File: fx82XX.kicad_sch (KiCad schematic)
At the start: 53 parts, among them J1 VBAT, J2 GND, J4 U1V10F5, J6 Raspberry_Pi_2_3, P1 Power Button, Q1 MMFTP3401, SW1 SW_Push, SW10 SW_Push, SW11 SW_Push, SW12 SW_Push, SW13 SW_Push, SW14 SW_Push, SW15 SW_Push, SW16 SW_Push, SW17 SW_Push, SW18 SW_Push, SW19 SW_Push, SW2 SW_Push, SW20 SW_Push, SW21 SW_Push, SW22 SW_Push, SW23 SW_Push, SW24 SW_Push, SW25 SW_Push, SW26 SW_Push, SW27 SW_Push, SW28 SW_Push, SW29 SW_Push, SW3 SW_Push, SW30 Previous, SW31 SW_Push, SW32 SW_Push, SW33 SW_Push, SW34 SW_Push, SW35 SW_Push, SW36 UpArrow, SW37 SW_Push, SW38 SW_Push, SW39 SW_Push, SW4 SW_Push, SW40 SW_Push, SW41 SW_Push, SW42 Home, SW43 SW_Push, SW44 SW_Push, SW45 SW_Push, SW46 SW_Push, SW47 SW_Push, SW5 SW_Push, SW6 SW_Push, SW7 SW_Push, SW8 SW_Push, SW9 SW_Push

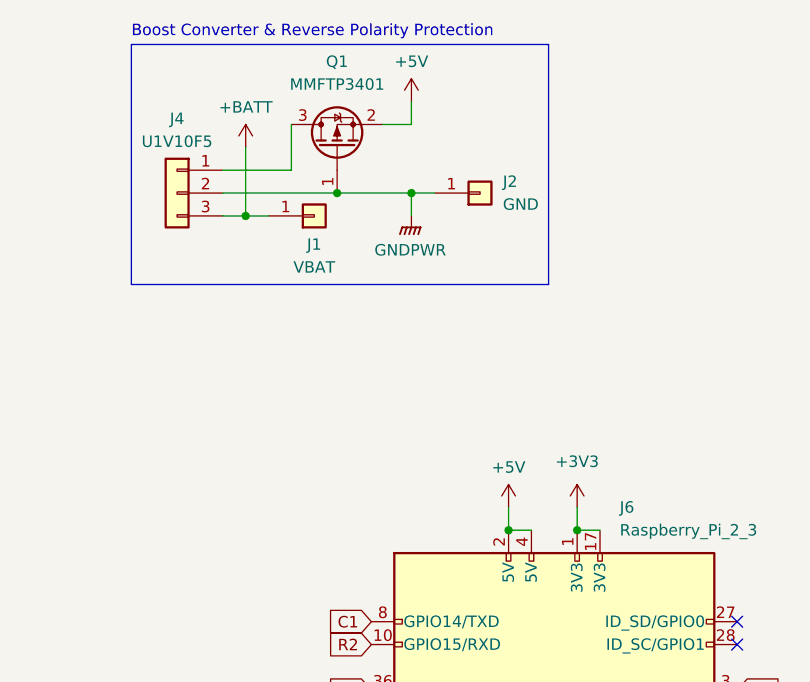
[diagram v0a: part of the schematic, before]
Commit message: Change symbol references
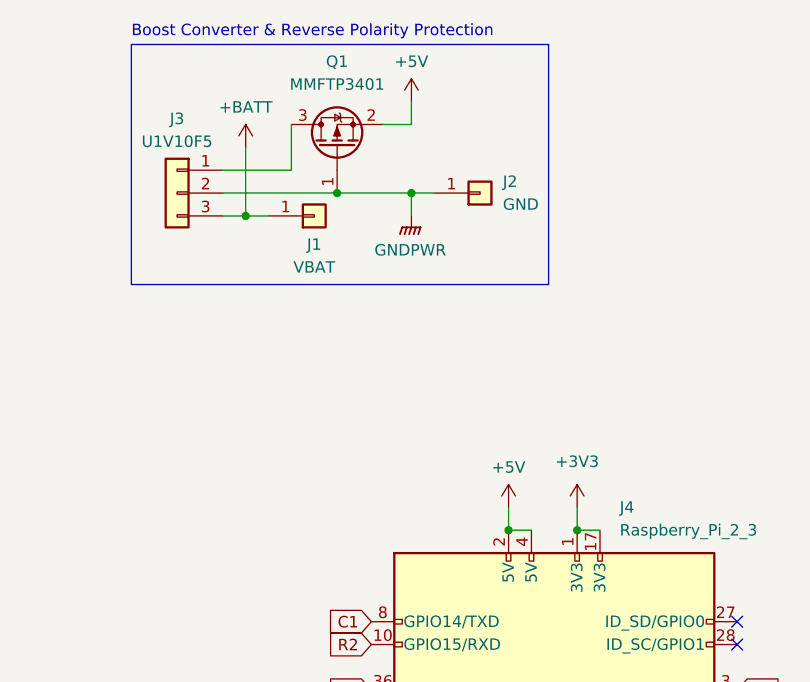
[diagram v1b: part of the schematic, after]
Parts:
- renumbered J4 to J3, J6 to J4
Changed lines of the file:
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@@
   (symbol (lib_id "Connector_Generic:Conn_01x03") (at 132.715 37.465 0) (mirror y) (unit 1)
     (in_bom yes) (on_board yes) (dnp no)
-    (property "Reference" "J4" (at 132.715 29.21 0)
+    (property "Reference" "J3" (at 132.715 29.21 0)
       (effects (font (size 1.27 1.27)))
     )
@@
       (project "fx82XX"
         (path "/d5effe3a-4045-4007-a8c8-6940eeb133a7"
-          (reference "J4") (unit 1)
+          (reference "J3") (unit 1)
         )
       )
@@
   (symbol (lib_id "Connector:Raspberry_Pi_2_3") (at 174.625 107.95 0) (unit 1)
     (in_bom yes) (on_board yes) (dnp no) (fields_autoplaced)
-    (property "Reference" "J6" (at 181.8991 72.39 0)
+    (property "Reference" "J4" (at 181.8991 72.39 0)
       (effects (font (size 1.27 1.27)) (justify left))
     )
@@
       (project "fx82XX"
         (path "/d5effe3a-4045-4007-a8c8-6940eeb133a7"
-          (reference "J6") (unit 1)
-        )
-      )
+          (reference "J4") (unit 1)
+        )
+      )

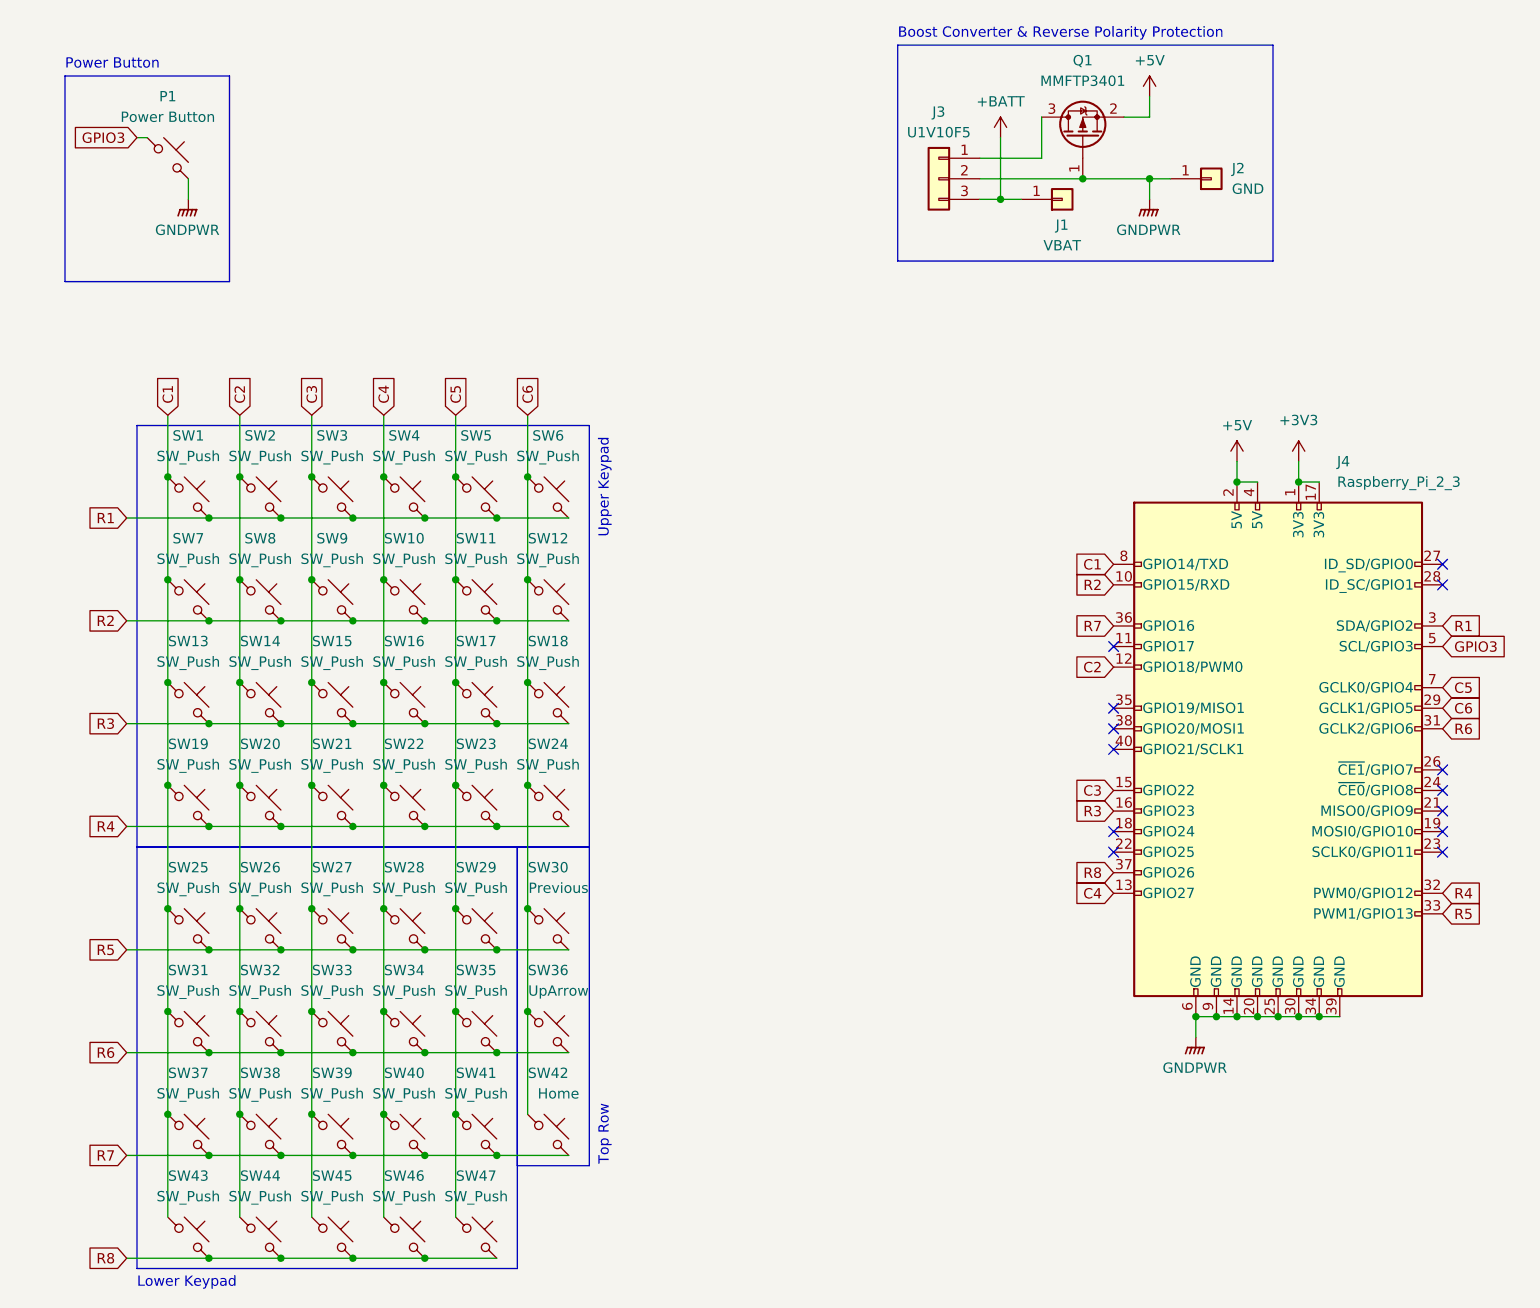
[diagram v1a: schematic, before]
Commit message: Re-route using 2 layers
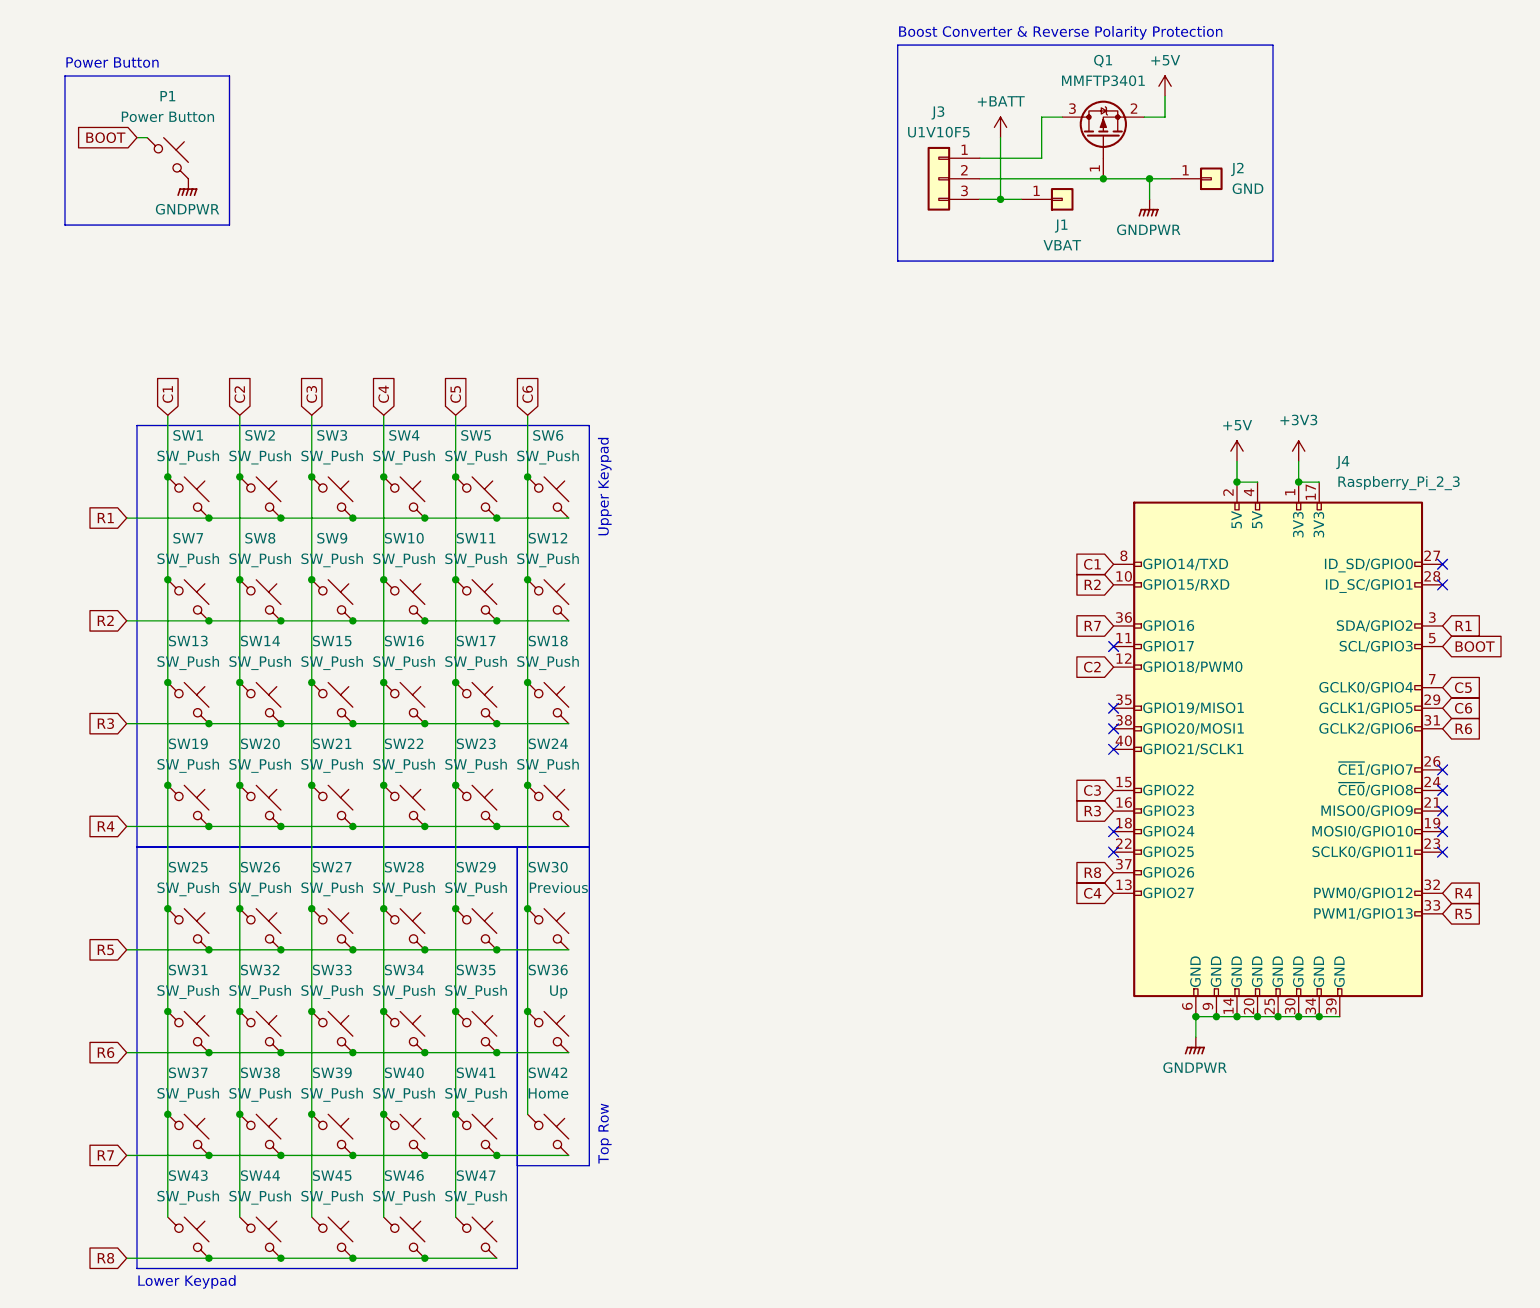
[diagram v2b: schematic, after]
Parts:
- SW36: value UpArrow -> Up
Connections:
- net GPIO3 renamed BOOT
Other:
- moved on the sheet: Q1

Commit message: Redesign PCB to be more accurate and better
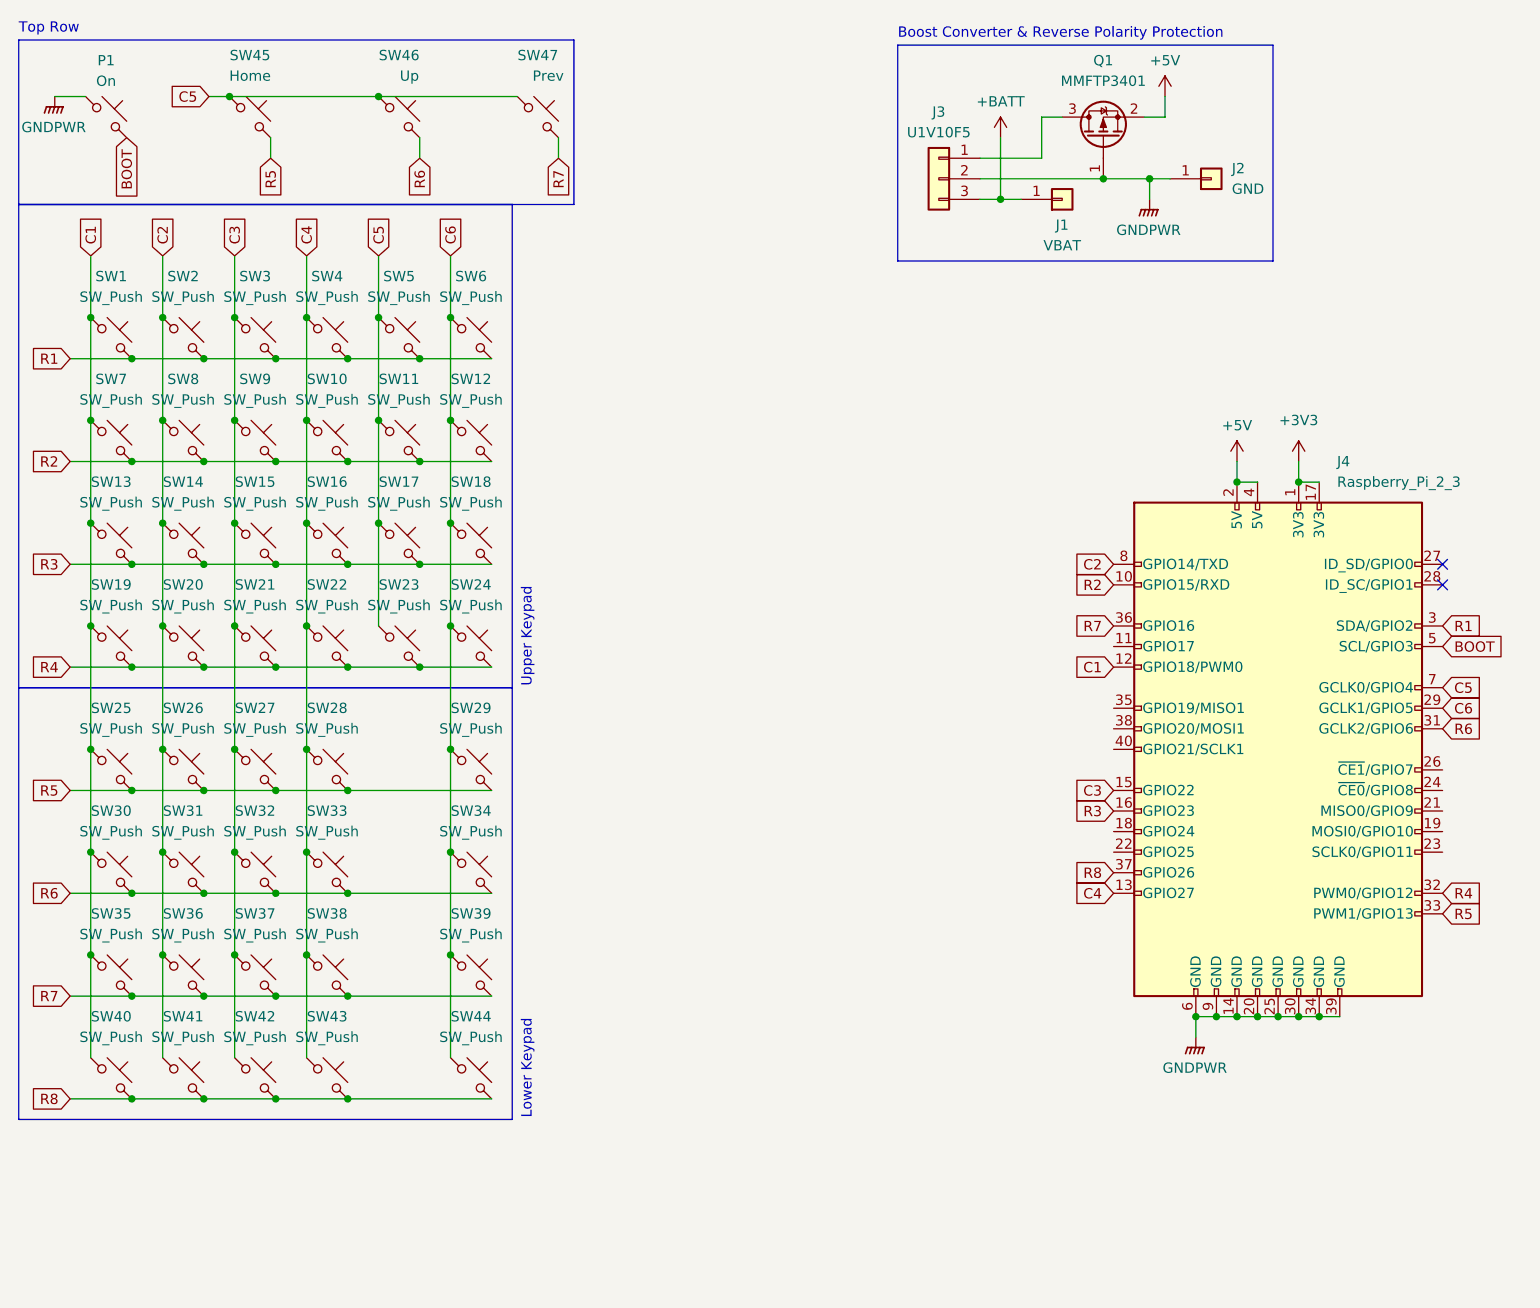
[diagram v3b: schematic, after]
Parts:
- J1, J2: footprint TestPoint:TestPoint_Pad_2.0x2.0mm -> TestPoint:TestPoint_Pad_3.0x3.0mm
- P1: value Power Button -> On
- SW47: renamed from SW30; value Previous -> Prev
- renumbered SW31 to SW30, SW32 to SW31, SW33 to SW32, SW34 to SW33, SW35 to SW34, SW37 to SW35, SW38 to SW36, SW39 to SW37, SW40 to SW38, SW41 to SW39, SW43 to SW40, SW44 to SW41, SW45 to SW42, SW46 to SW43, SW47 to SW44, SW42 to SW45, SW36 to SW46
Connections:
- net BOOT: now also P1.2; no longer P1.1
- net C1: now also J4.12 (GPIO18/PWM0); no longer J4.8 (GPIO14/TXD)
- net C2: now also J4.8 (GPIO14/TXD); no longer J4.12 (GPIO18/PWM0)
- net C5: now also SW45.1, SW46.1, SW47.1; no longer SW29.1, SW34.1, SW39.1, SW44.1
- net C6: now also SW29.1, SW34.1, SW39.1, SW44.1; no longer SW45.1, SW46.1, SW47.1
- net GNDPWR: now also P1.1; no longer P1.2
- net R5: now also SW45.2; no longer SW47.2
- net R7: now also SW47.2; no longer SW45.2
- no-connect marks 13 -> 2
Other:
- note removed: "Power Button"
- moved on the sheet: P1, SW1, SW10, SW11, SW12, SW13, SW14, SW15, SW16, SW17, SW18, SW19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
